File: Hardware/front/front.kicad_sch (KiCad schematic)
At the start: 55 parts, among them J101 Conn_02x10_Odd_Even, SW101 TT EN11, SW102 B3W-9002-G1G, SW103 B3W-9002-Y1C, SW104 B3W-9002-Y1C, SW105 B3W-9002-Y1C, SW106 B3W-9002-Y1C, SW107 B3W-9000-RHG2C, U101 XRA1203, U102 AT24CS32-SSHM, U103 PCA9955B, U104 74LV14, U105 74LVC1G14GV

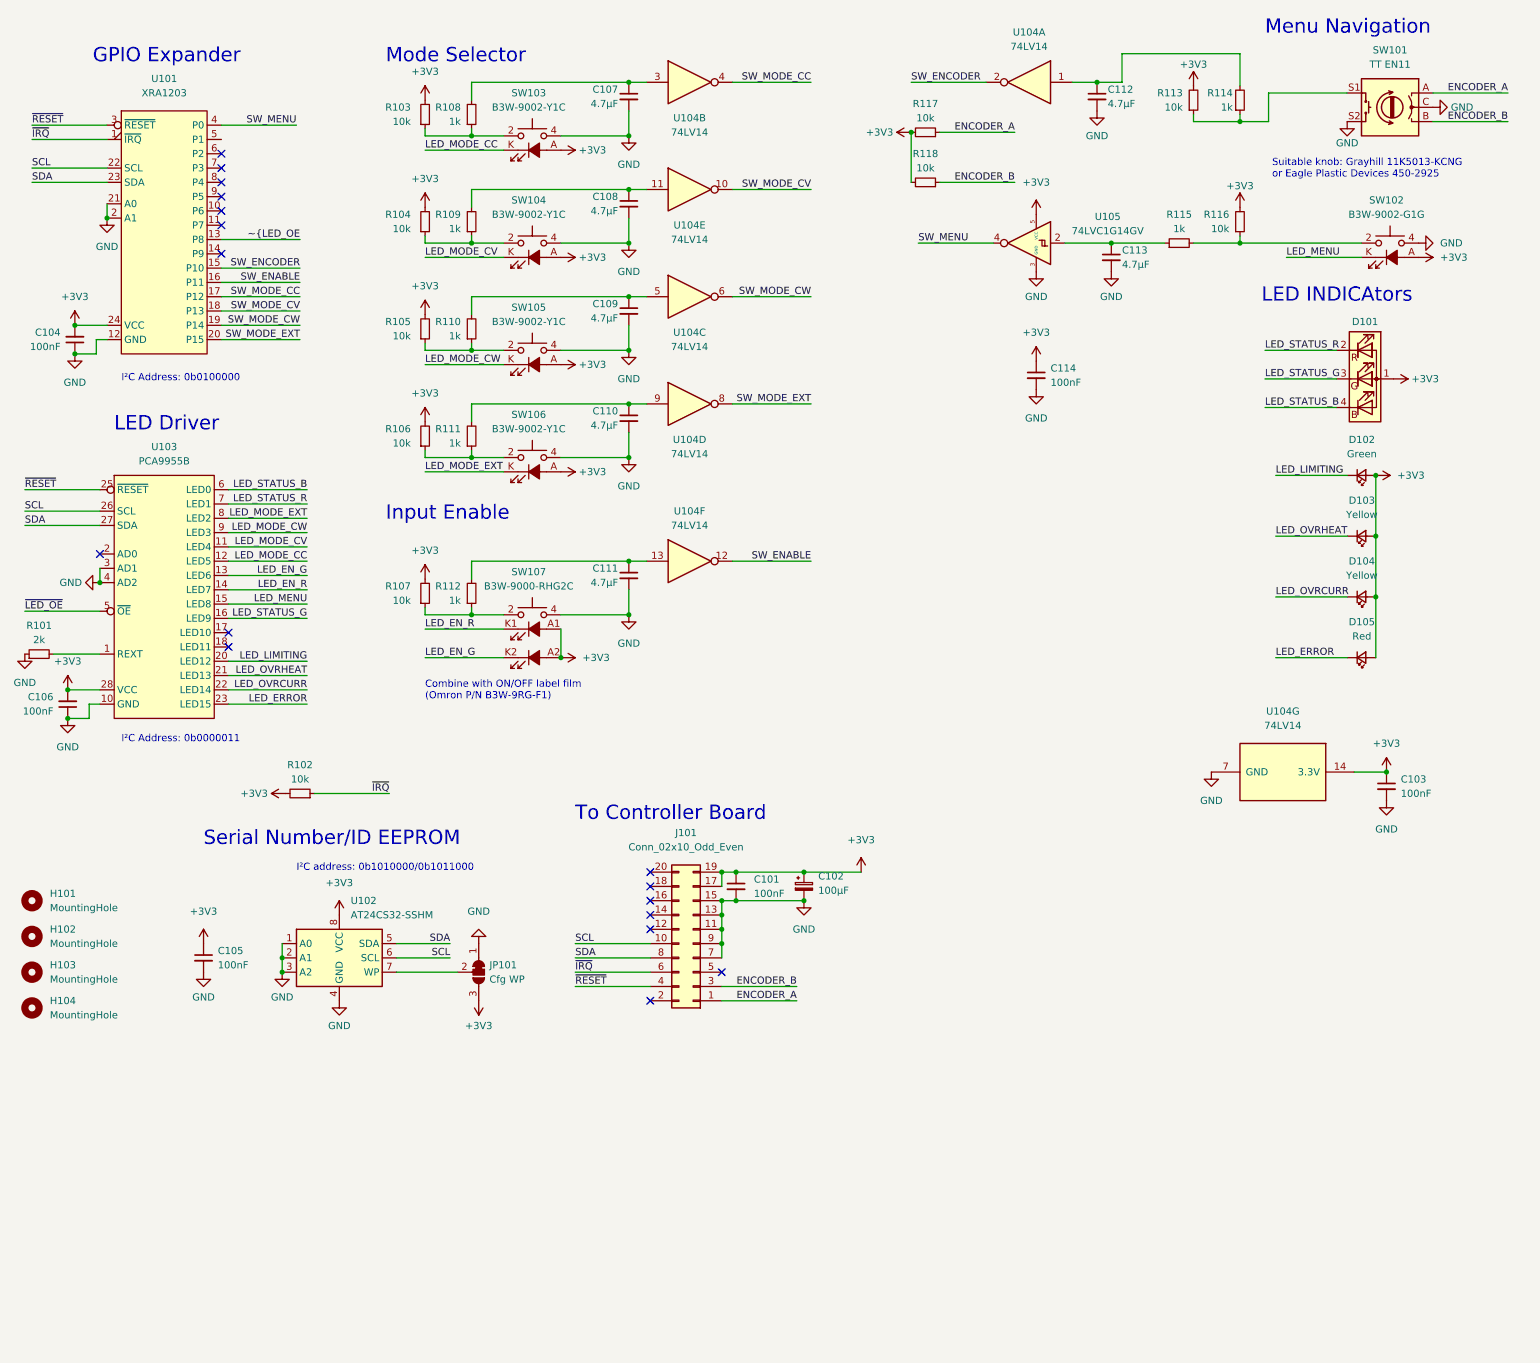
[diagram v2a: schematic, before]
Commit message: Start reworking front panel board
- Embiggen the board to hold the TFT display (which replaces the small
  graphical OLED) to display stuff on the front panel

- Moved some of the switches and screw holes around to better fit

- Changed screws from M2.5 to M3

- Added footprint for ER-TFT040-1 display; this is only the mechanical
  outline - no actual contacts. You should place an FFC connector
  separately on the board where indicated.
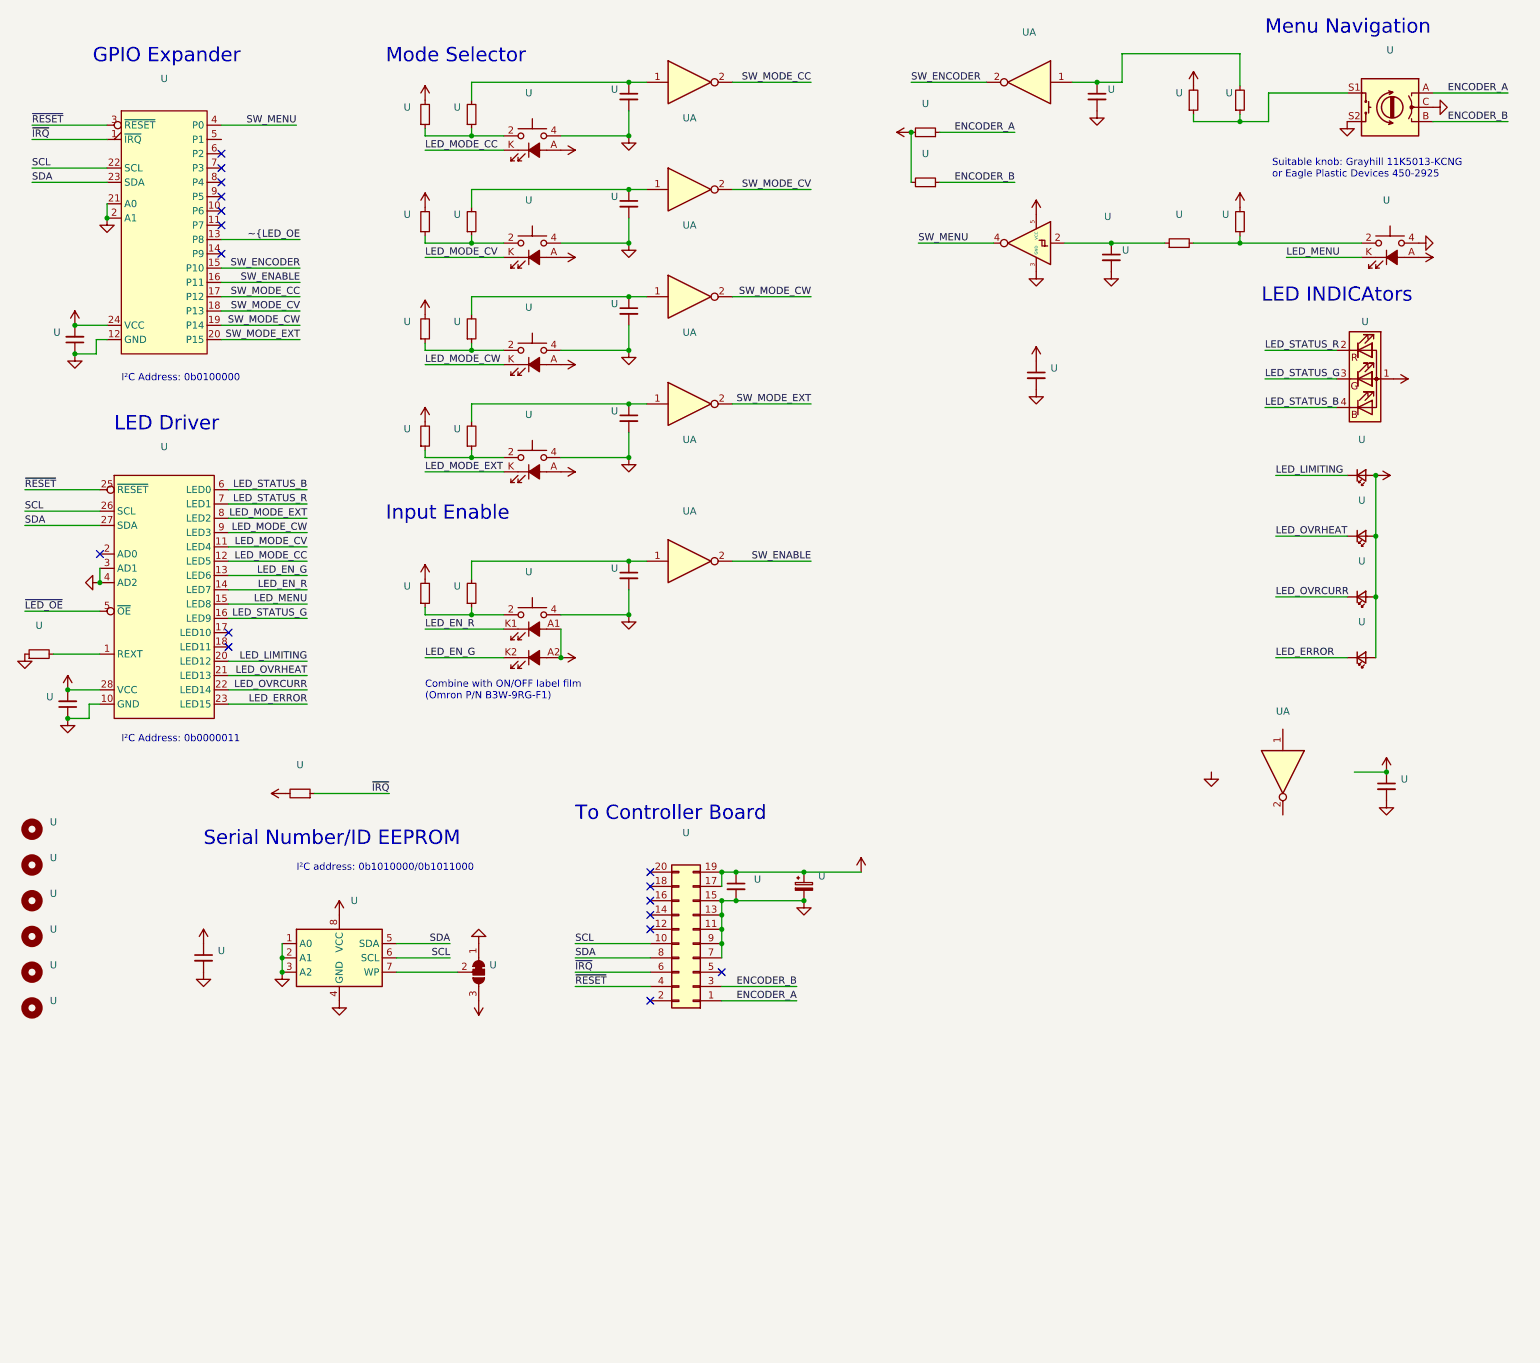
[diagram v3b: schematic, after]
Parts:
- added U (x2): (no value), symbol Mechanical:MountingHole
- U: renamed from H102; value MountingHole -> (none); footprint MountingHole:MountingHole_2.7mm_M2.5 -> (none)
- U: renamed from SW103; value B3W-9002-Y1C -> (none); footprint programmable-load:Omron-B3W-90XX-X1X -> (none)
- U: renamed from C111; value 4.7µF -> (none); footprint Capacitor_SMD:C_0805_2012Metric_Pad1.18x1.45mm_HandSolder -> (none)
- U: renamed from C106; value 100nF -> (none); footprint Capacitor_SMD:C_0805_2012Metric_Pad1.18x1.45mm_HandSolder -> (none)
- U: renamed from U104; value 74LV14 -> (none); footprint Package_SO:TSSOP-14_4.4x5mm_P0.65mm -> (none)
- U: renamed from R114; value 1k -> (none); footprint Resistor_SMD:R_0805_2012Metric_Pad1.20x1.40mm_HandSolder -> (none)
- U: renamed from C109; value 4.7µF -> (none); footprint Capacitor_SMD:C_0805_2012Metric_Pad1.18x1.45mm_HandSolder -> (none)
- U: renamed from H104; value MountingHole -> (none); footprint MountingHole:MountingHole_2.7mm_M2.5 -> (none)
- U: renamed from H103; value MountingHole -> (none); footprint MountingHole:MountingHole_2.7mm_M2.5 -> (none)
- U: renamed from U102; value AT24CS32-SSHM -> (none); footprint Package_SO:SOIC-8_3.9x4.9mm_P1.27mm -> (none)
- U: renamed from R109; value 1k -> (none); footprint Resistor_SMD:R_0805_2012Metric_Pad1.20x1.40mm_HandSolder -> (none)
- U: renamed from R106; value 10k -> (none); footprint Resistor_SMD:R_0805_2012Metric_Pad1.20x1.40mm_HandSolder -> (none)
- U: renamed from D101; value LED_RGBA -> (none); footprint LED_SMD:LED_RGB_1210 -> (none)
- U: renamed from C101; value 100nF -> (none); footprint Capacitor_SMD:C_0805_2012Metric_Pad1.18x1.45mm_HandSolder -> (none)
- U: renamed from C110; value 4.7µF -> (none); footprint Capacitor_SMD:C_0805_2012Metric_Pad1.18x1.45mm_HandSolder -> (none)
- U: renamed from JP101; value Cfg WP -> (none); footprint Jumper:SolderJumper-3_P1.3mm_Bridged12_RoundedPad1.0x1.5mm -> (none)
- U: renamed from R112; value 1k -> (none); footprint Resistor_SMD:R_0805_2012Metric_Pad1.20x1.40mm_HandSolder -> (none)
- U: renamed from U105; value 74LVC1G14GV -> (none); footprint Package_TO_SOT_SMD:SOT-23-5 -> (none)
- U: renamed from R104; value 10k -> (none); footprint Resistor_SMD:R_0805_2012Metric_Pad1.20x1.40mm_HandSolder -> (none)
- U: renamed from R110; value 1k -> (none); footprint Resistor_SMD:R_0805_2012Metric_Pad1.20x1.40mm_HandSolder -> (none)
- U: renamed from J101; value Conn_02x10_Odd_Even -> (none); footprint Connector_PinHeader_1.27mm:PinHeader_2x10_P1.27mm_Vertical_SMD -> (none)
- U: renamed from R107; value 10k -> (none); footprint Resistor_SMD:R_0805_2012Metric_Pad1.20x1.40mm_HandSolder -> (none)
- U: renamed from SW102; value B3W-9002-G1G -> (none); footprint programmable-load:Omron-B3W-90XX-X1X -> (none)
- U: renamed from R113; value 10k -> (none); footprint Resistor_SMD:R_0805_2012Metric_Pad1.20x1.40mm_HandSolder -> (none)
- U: renamed from U101; value XRA1203 -> (none); footprint Package_SO:TSSOP-24_4.4x7.8mm_P0.65mm -> (none)
- U: renamed from C112; value 4.7µF -> (none); footprint Capacitor_SMD:C_0805_2012Metric_Pad1.18x1.45mm_HandSolder -> (none)
- U: renamed from R115; value 1k -> (none); footprint Resistor_SMD:R_0805_2012Metric_Pad1.20x1.40mm_HandSolder -> (none)
- U: renamed from R118; value 10k -> (none); footprint Resistor_SMD:R_0805_2012Metric_Pad1.20x1.40mm_HandSolder -> (none)
- U: renamed from C113; value 4.7µF -> (none); footprint Capacitor_SMD:C_0805_2012Metric_Pad1.18x1.45mm_HandSolder -> (none)
- U: renamed from SW104; value B3W-9002-Y1C -> (none); footprint programmable-load:Omron-B3W-90XX-X1X -> (none)
- U: renamed from SW101; value TT EN11 -> (none); footprint programmable-load:TT_Electronics-EN11-HSM1AF15-0 -> (none)
- U: renamed from C104; value 100nF -> (none); footprint Capacitor_SMD:C_0805_2012Metric_Pad1.18x1.45mm_HandSolder -> (none)
- U: renamed from D102; value Green -> (none); footprint LED_SMD:LED_1206_3216Metric_Pad1.42x1.75mm_HandSolder -> (none)
- U: renamed from D104; value Yellow -> (none); footprint LED_SMD:LED_1206_3216Metric_Pad1.42x1.75mm_HandSolder -> (none)
- U: renamed from R116; value 10k -> (none); footprint Resistor_SMD:R_0805_2012Metric_Pad1.20x1.40mm_HandSolder -> (none)
- U: renamed from C102; value 100µF -> (none); footprint Capacitor_SMD:CP_Elec_5x5.3 -> (none)
- U: renamed from SW106; value B3W-9002-Y1C -> (none); footprint programmable-load:Omron-B3W-90XX-X1X -> (none)
- U: renamed from R103; value 10k -> (none); footprint Resistor_SMD:R_0805_2012Metric_Pad1.20x1.40mm_HandSolder -> (none)
- U: renamed from C108; value 4.7µF -> (none); footprint Capacitor_SMD:C_0805_2012Metric_Pad1.18x1.45mm_HandSolder -> (none)
- U: renamed from U103; value PCA9955B -> (none); footprint Package_SO:HTSSOP-28-1EP_4.4x9.7mm_P0.65mm_EP2.85x5.4mm_ThermalVias -> (none)
- U: renamed from R105; value 10k -> (none); footprint Resistor_SMD:R_0805_2012Metric_Pad1.20x1.40mm_HandSolder -> (none)
- U: renamed from R117; value 10k -> (none); footprint Resistor_SMD:R_0805_2012Metric_Pad1.20x1.40mm_HandSolder -> (none)
- U: renamed from C103; value 100nF -> (none); footprint Capacitor_SMD:C_0805_2012Metric_Pad1.18x1.45mm_HandSolder -> (none)
- U: renamed from D103; value Yellow -> (none); footprint LED_SMD:LED_1206_3216Metric_Pad1.42x1.75mm_HandSolder -> (none)
- U: renamed from H101; value MountingHole -> (none); footprint MountingHole:MountingHole_2.7mm_M2.5 -> (none)
- U: renamed from C107; value 4.7µF -> (none); footprint Capacitor_SMD:C_0805_2012Metric_Pad1.18x1.45mm_HandSolder -> (none)
- U: renamed from R102; value 10k -> (none); footprint Resistor_SMD:R_0805_2012Metric_Pad1.20x1.40mm_HandSolder -> (none)
- U: renamed from C105; value 100nF -> (none); footprint Capacitor_SMD:C_0805_2012Metric_Pad1.18x1.45mm_HandSolder -> (none)
- U: renamed from D105; value Red -> (none); footprint LED_SMD:LED_1206_3216Metric_Pad1.42x1.75mm_HandSolder -> (none)
- U: renamed from SW105; value B3W-9002-Y1C -> (none); footprint programmable-load:Omron-B3W-90XX-X1X -> (none)
- U: renamed from R108; value 1k -> (none); footprint Resistor_SMD:R_0805_2012Metric_Pad1.20x1.40mm_HandSolder -> (none)
- U: renamed from SW107; value B3W-9000-RHG2C -> (none); footprint programmable-load:Omron-B3W-90XX-X2X -> (none)
- U: renamed from R101; value 2k -> (none); footprint Resistor_SMD:R_0805_2012Metric_Pad1.20x1.40mm_HandSolder -> (none)
- U: renamed from R111; value 1k -> (none); footprint Resistor_SMD:R_0805_2012Metric_Pad1.20x1.40mm_HandSolder -> (none)
- U: renamed from C114; value 100nF -> (none); footprint Capacitor_SMD:C_0805_2012Metric_Pad1.18x1.45mm_HandSolder -> (none)
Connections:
- net +3V3: no longer U.14 (3.3V)
- net GND: no longer U.7 (GND)
- net SW_ENABLE: now also U.2; no longer U.12
- net SW_MODE_CC: now also U.2; no longer U.4
- net SW_MODE_CV: now also U.2; no longer U.10
- net SW_MODE_CW: now also U.2; no longer U.6
- net SW_MODE_EXT: now also U.2; no longer U.8
- net at U.1, U.2: now also U.1; no longer U.13
- net at U.1, U.2: now also U.1; no longer U.5
- net at U.1, U.2: now also U.1; no longer U.11
- net at U.1, U.2: now also U.1; no longer U.9
- net at U.1, U.2: now also U.1; no longer U.3
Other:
- moved on the sheet: U

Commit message: More front panel work
- Split the front panel into multiple separate sheets (for easier
  dealing with since there's now more stuff)

- Added FFC connectors for display, connection to main board

- Start routing some of these connections
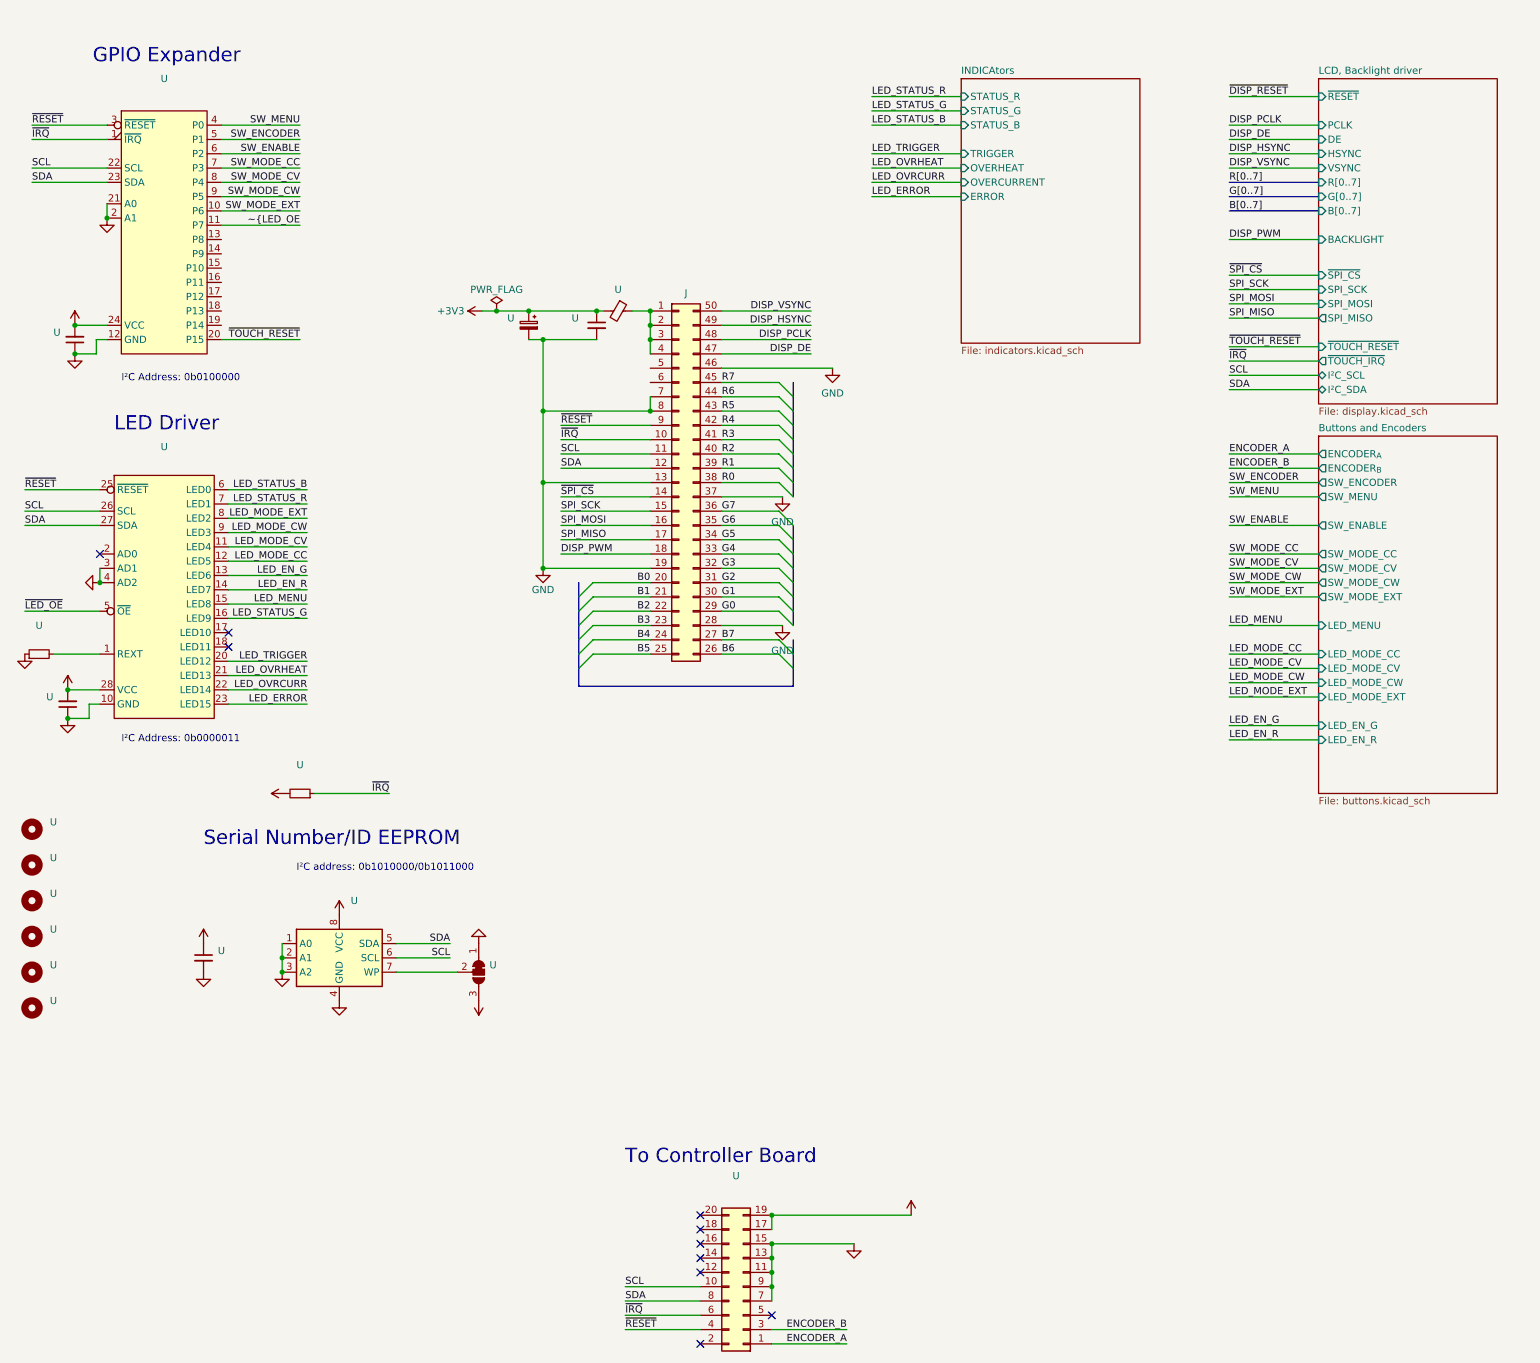
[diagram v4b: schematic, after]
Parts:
- removed U (x5): (no value), symbol programmable-load:B3W-900X-X1X
- removed U (x9): (no value), symbol Device:C_Small
- removed U (x7): (no value), symbol 74xx:74LV14
- removed U (x16): (no value), symbol Device:R_Small
- removed U: (no value), symbol Device:LED_ARGB
- removed U: (no value), symbol 74xGxx:SN74LVC1G14DBV
- removed U: (no value), symbol Device:RotaryEncoder_Switch
- removed U (x4): (no value), symbol Device:LED_Small
- removed U: (no value), symbol programmable-load:B3W-900X-X2X
- added J: Conn_02x25_Counter_Clockwise, symbol Connector_Generic:Conn_02x25_Counter_Clockwise
- added U: (no value), symbol Device:FerriteBead_Small
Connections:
- net +3V3: now also U.2
- net GND: now also J.13 (Pin_13), J.19 (Pin_19), J.28 (Pin_28), J.37 (Pin_37), J.46 (Pin_46), J.7 (Pin_7), J.8 (Pin_8)
- net SCL: now also J.11 (Pin_11)
- net SDA: now also J.12 (Pin_12)
- net SW_ENABLE: now also U.6 (P2); no longer U.16 (P11)
- net SW_ENCODER: now also U.5 (P1); no longer U.15 (P10)
- net SW_MODE_CC: now also U.7 (P3); no longer U.17 (P12)
- net SW_MODE_CV: now also U.8 (P4); no longer U.18 (P13)
- net SW_MODE_CW: now also U.9 (P5); no longer U.19 (P14)
- net SW_MODE_EXT: now also U.10 (P6); no longer U.20 (P15)
- net ~{IRQ}: now also J.10 (Pin_10)
- net ~{LED_OE: now also U.11 (P7); no longer U.13 (P8)
- net ~{RESET}: now also J.9 (Pin_9)
- net LED_LIMITING renamed LED_TRIGGER
- new net: J.1 (Pin_1), J.2 (Pin_2), J.3 (Pin_3), J.4 (Pin_4), U.1
- new net B0: J.20 (Pin_20)
- new net B1: J.21 (Pin_21)
- new net B2: J.22 (Pin_22)
- new net B3: J.23 (Pin_23)
- new net B4: J.24 (Pin_24)
- new net B5: J.25 (Pin_25)
- new net B6: J.26 (Pin_26)
- new net B7: J.27 (Pin_27)
- new net DISP_DE: J.47 (Pin_47)
- new net DISP_HSYNC: J.49 (Pin_49)
- new net DISP_PCLK: J.48 (Pin_48)
- new net DISP_PWM: J.18 (Pin_18)
- new net DISP_VSYNC: J.50 (Pin_50)
- new net G0: J.29 (Pin_29)
- new net G1: J.30 (Pin_30)
- new net G2: J.31 (Pin_31)
- new net G3: J.32 (Pin_32)
- new net G4: J.33 (Pin_33)
- new net G5: J.34 (Pin_34)
- new net G6: J.35 (Pin_35)
- new net G7: J.36 (Pin_36)
- new net R0: J.38 (Pin_38)
- new net R1: J.39 (Pin_39)
- new net R2: J.40 (Pin_40)
- new net R3: J.41 (Pin_41)
- new net R4: J.42 (Pin_42)
- new net R5: J.43 (Pin_43)
- new net R6: J.44 (Pin_44)
- new net R7: J.45 (Pin_45)
- new net SPI_MISO: J.17 (Pin_17)
- new net SPI_MOSI: J.16 (Pin_16)
- new net SPI_SCK: J.15 (Pin_15)
- new net ~{SPI_CS}: J.14 (Pin_14)
- new net ~{TOUCH_RESET}: U.20 (P15)
- no-connect marks 17 -> 10
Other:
- added sheet Buttons and Encoders (buttons.kicad_sch)
- added sheet INDICAtors (indicators.kicad_sch)
- added sheet LCD, Backlight driver (display.kicad_sch)
- note removed: "Combine with ON/OFF label film (Omron P/N B3W-9RG-F1)"
- note removed: "Input Enable"
- note removed: "LED INDICAtors"
- note removed: "Menu Navigation"
- note removed: "Mode Selector"
- note removed: "Suitable knob: Grayhill 11K5013-KCNG or Eagle Plastic Devices 450-2925"
- moved on the sheet: U
